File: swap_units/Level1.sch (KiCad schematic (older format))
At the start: 3 parts, among them U1 LM324

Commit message: Refreshed test suite
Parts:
- U1: footprint Package_DIP:DIP-14_W7.62mm -> (none)
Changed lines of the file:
@@
 EESchema Schematic File Version 4
-EELAYER 26 0
+LIBS:swap_units_test-cache
+EELAYER 29 0
 EELAYER END
 $Descr A4 11693 8268
@@
 F2 "out_level_2" O R 4150 5100 50
 $EndSheet
-$Comp
-L Amplifier_Operational:LM324 U1
-U 3 1 5B2A178A
-P 3300 3550
-F 0 "U1" H 3300 3750 50  0000 L CNN
-F 1 "LM324" H 3300 3350 50  0000 L CNN
-F 2 "Package_DIP:DIP-14_W7.62mm" H 3250 3650 50  0001 C CNN
-F 3 "http://www.ti.com/lit/ds/symlink/lm2902-n.pdf" H 3350 3750 50  0001 C CNN
-	3    3300 3550
-	1    0    0    -1
-$EndComp
 $Comp
 L Device:R R4
@@
 Text HLabel 4450 5100 2    50   Output ~ 0
 out_level_2
+$Comp
+L Amplifier_Operational:LM324 U1
+U 3 1 5C8869E5
+P 3300 3550
+F 0 "U1" H 3300 3750 50  0000 L CNN
+F 1 "LM324" H 3300 3350 50  0000 L CNN
+F 2 "" H 3250 3650 50  0001 C CNN
+F 3 "http://www.ti.com/lit/ds/symlink/lm2902-n.pdf" H 3350 3750 50  0001 C CNN
+	3    3300 3550
+	1    0    0    -1
+$EndComp
 $EndSCHEMATC

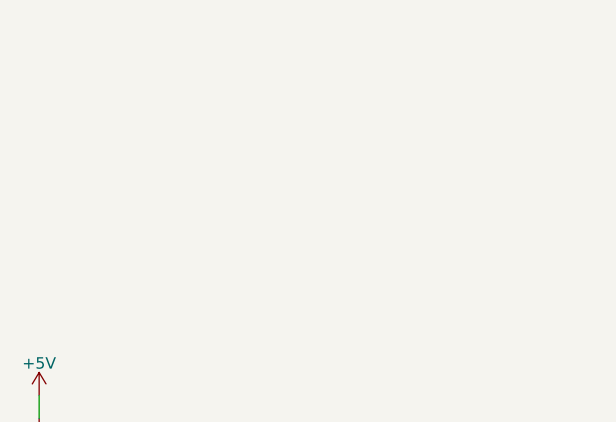
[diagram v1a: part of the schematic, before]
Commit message: Updated test project to include multiple hierarchy
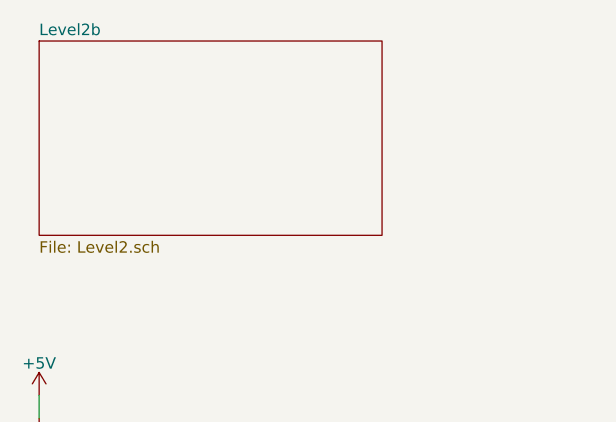
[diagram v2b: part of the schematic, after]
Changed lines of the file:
@@
 $Descr A4 11693 8268
 encoding utf-8
-Sheet 2 3
+Sheet 2 4
 Title ""
 Date ""
@@
 	1    0    0    -1
 $EndComp
+$Sheet
+S 2550 1300 1500 850
+U 5C9CDC4B
+F0 "Level2b" 50
+F1 "Level2.sch" 50
+$EndSheet
 $EndSCHEMATC
